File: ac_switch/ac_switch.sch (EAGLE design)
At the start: 7 parts, among them IC1 LM358D, T1 BC337

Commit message: schaltung AC-Switch 98% fertig
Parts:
- added C3, C5: 100n, resistor:C-EU025-024X044
- added C4: 470µ, resistor:CPOL-EUE2.5-7
- added LED1: (no value), led:LED5MM
- added LSP1, LSP2, LSP3, LSP4, LSP5, LSP6: SE14, solpad:SE14
- added R1: 10K, resistor:R-EU_0207/10
- added R2: 150R, resistor:R-EU_0207/10
- added U$3: I3C_PORT, n39:I3C_PORT
- added U$4: AVR_ISP, n39:AVR_ISP
- added X1: SSW-103-02-S-S-RA, con-samtec:SSW-103-02-S-S-RA
- IC1: value LM358D -> TINY85; device linear:LM358D -> atmel:TINY22P
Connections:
- new net L: LSP1.MP, LSP4.MP, U$2.IP+
- new net L_OUT: U$1.P$3, X1-3.1
- new net N: LSP2.MP, LSP5.MP, X1-2.1
- new net N$5: LED1.A, R2.2
- new net P: LSP3.MP, LSP6.MP, X1-1.1
- new net REQ: IC1.(MISO)PB1, U$3.REQ, U$4.MISO
- new net RST: IC1.RESET, R1.2, U$4.RST
- new net SCL: IC1.(SCK)PB2, U$3.SCL, U$4.SCK
- new net SDA: IC1.(MOSI)PB0, U$3.SDA, U$4.MOSI
- net GND: now also C3.1, C4.-, C5.2, IC1.GND, LED1.C
- net N$1: now also R2.1
- net SENSE: now also IC1.(CLOCK)PB3
- net SWITCH: now also IC1.PB4
- net VCC: now also C3.2, C4.+, C5.1, IC1.VCC, R1.1
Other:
- note added: "230VAC"
- note added: "5VDC"
- note removed: "Schmitt-Trigger 0.3V"

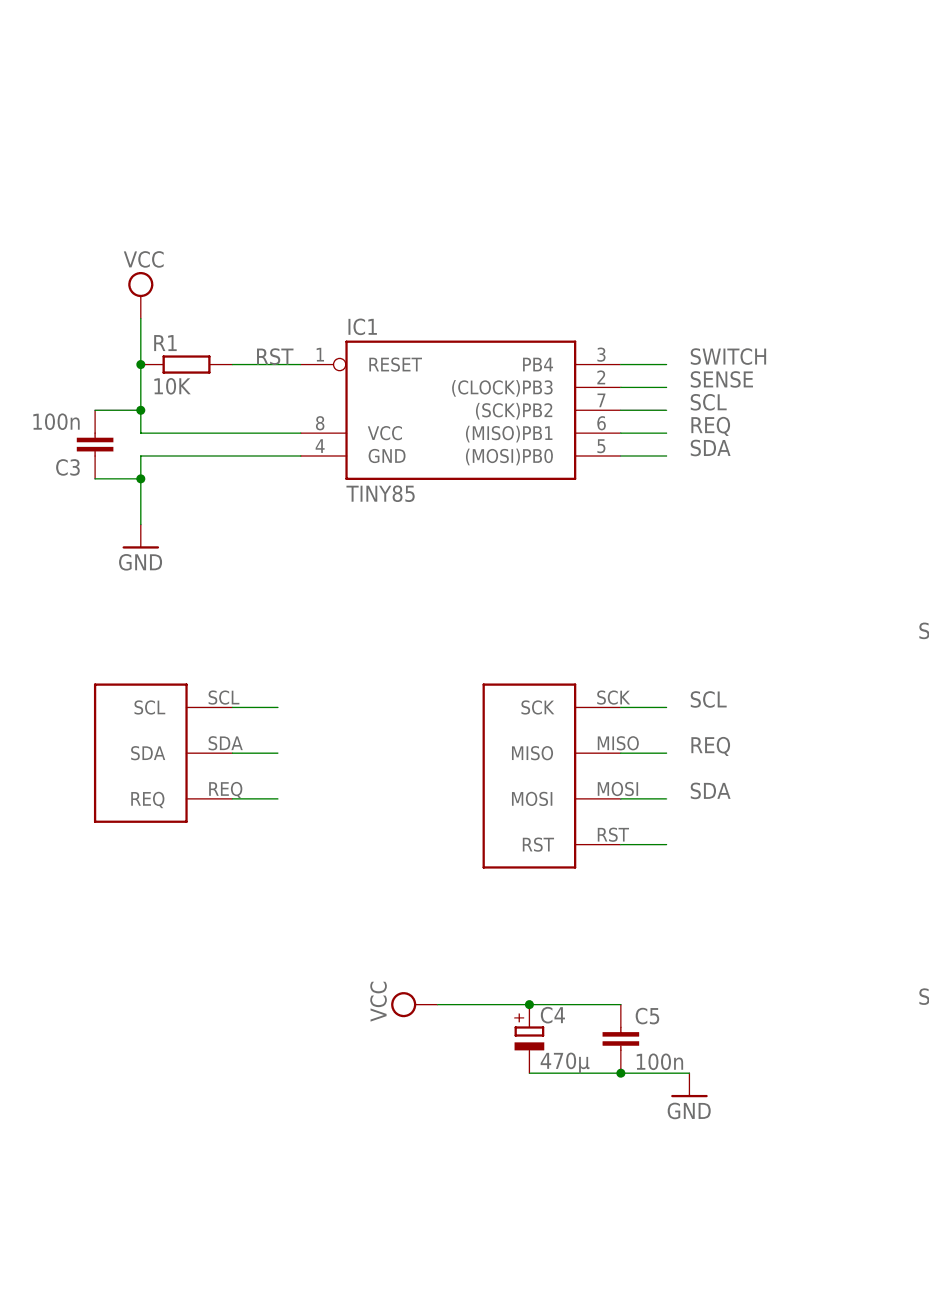
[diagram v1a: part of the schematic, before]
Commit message: weiterer I³C-Port
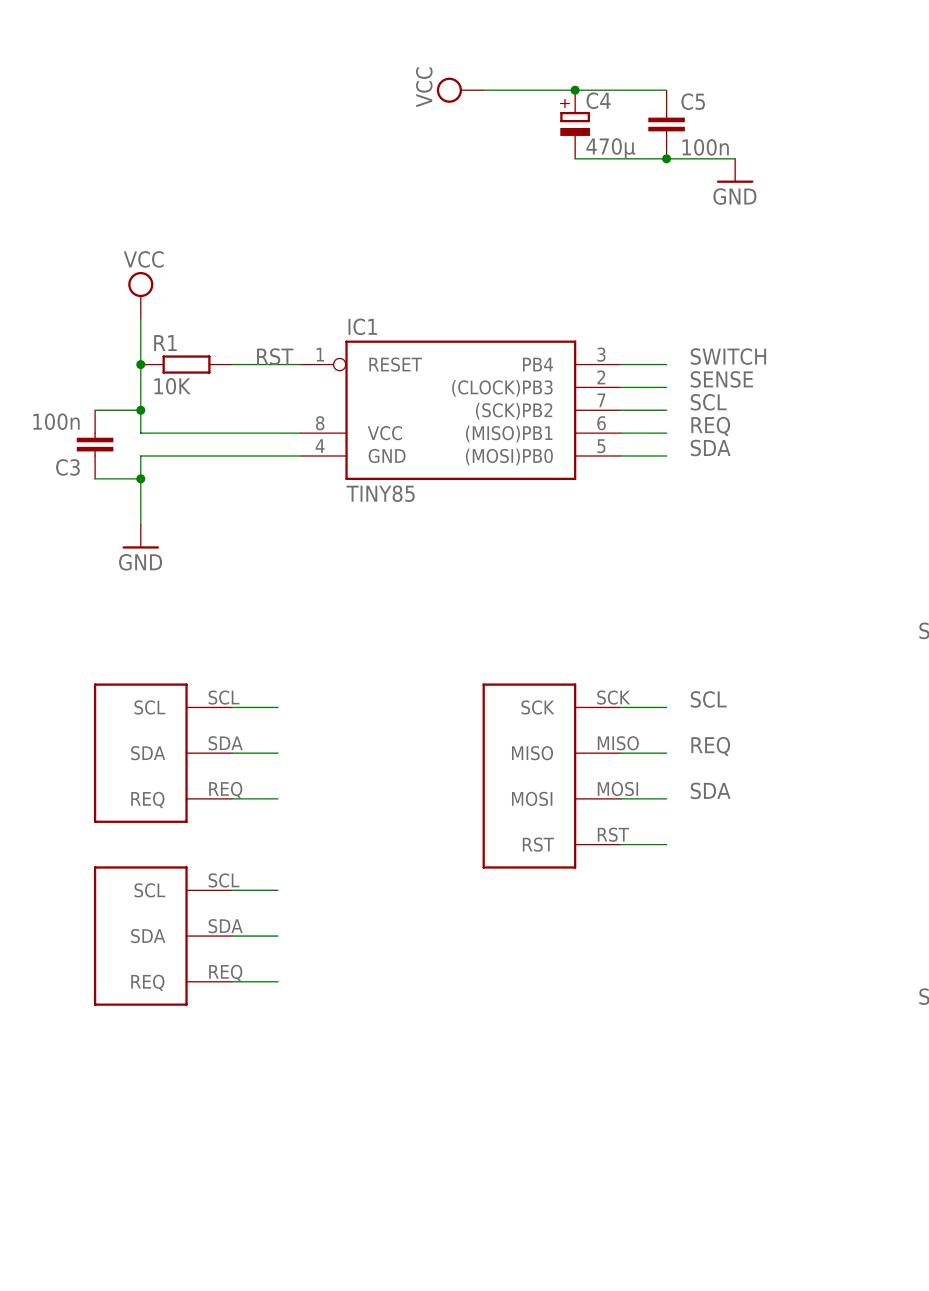
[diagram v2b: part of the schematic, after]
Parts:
- added U$5: I3C_PORT, n39:I3C_PORT
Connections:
- net REQ: now also U$5.REQ
- net SCL: now also U$5.SCL
- net SDA: now also U$5.SDA
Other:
- moved on the sheet: C4, C5
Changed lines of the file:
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@@
 <part name="C4" library="resistor" deviceset="CPOL-EU" device="E2.5-7" value="470µ"/>
 <part name="C5" library="resistor" deviceset="C-EU" device="025-024X044" value="100n"/>
+<part name="U$5" library="n39" deviceset="I3C_PORT" device=""/>
 </parts>
 <sheets>
@@
 <instance part="LSP6" gate="1" x="119.38" y="35.56" rot="R180"/>
 <instance part="GND1" gate="1" x="50.8" y="-38.1"/>
-<instance part="GND4" gate="1" x="0" y="-33.02"/>
-<instance part="SUPPLY4" gate="G$1" x="-30.48" y="-22.86" rot="R90"/>
-<instance part="C4" gate="G$1" x="-17.78" y="-25.4"/>
-<instance part="C5" gate="G$1" x="-7.62" y="-25.4"/>
+<instance part="GND4" gate="1" x="5.08" y="68.58"/>
+<instance part="SUPPLY4" gate="G$1" x="-25.4" y="78.74" rot="R90"/>
+<instance part="C4" gate="G$1" x="-12.7" y="76.2"/>
+<instance part="C5" gate="G$1" x="-2.54" y="76.2"/>
+<instance part="U$5" gate="G$1" x="-60.96" y="-17.78"/>
 </instances>
 <busses>
@@
 <pinref part="SUPPLY4" gate="G$1" pin="VCC"/>
 <pinref part="C4" gate="G$1" pin="+"/>
-<wire x1="-27.94" y1="-22.86" x2="-17.78" y2="-22.86" width="0.1524" layer="91"/>
-<wire x1="-17.78" y1="-22.86" x2="-7.62" y2="-22.86" width="0.1524" layer="91"/>
-<junction x="-17.78" y="-22.86"/>
+<wire x1="-22.86" y1="78.74" x2="-12.7" y2="78.74" width="0.1524" layer="91"/>
+<wire x1="-12.7" y1="78.74" x2="-2.54" y2="78.74" width="0.1524" layer="91"/>
+<junction x="-12.7" y="78.74"/>
 <pinref part="C5" gate="G$1" pin="1"/>
 </segment>
@@
 <pinref part="C4" gate="G$1" pin="-"/>
 <pinref part="GND4" gate="1" pin="GND"/>
-<wire x1="-17.78" y1="-30.48" x2="-7.62" y2="-30.48" width="0.1524" layer="91"/>
+<wire x1="-12.7" y1="71.12" x2="-2.54" y2="71.12" width="0.1524" layer="91"/>
 <pinref part="C5" gate="G$1" pin="2"/>
-<wire x1="-7.62" y1="-30.48" x2="0" y2="-30.48" width="0.1524" layer="91"/>
-<junction x="-7.62" y="-30.48"/>
+<wire x1="-2.54" y1="71.12" x2="5.08" y2="71.12" width="0.1524" layer="91"/>
+<junction x="-2.54" y="71.12"/>
 </segment>
 </net>
@@
 <label x="0" y="10.16" size="1.778" layer="95"/>
 </segment>
+<segment>
+<pinref part="U$5" gate="G$1" pin="SCL"/>
+<wire x1="-50.8" y1="-10.16" x2="-45.72" y2="-10.16" width="0.1524" layer="91"/>
+</segment>
 </net>
 <net name="REQ" class="0">
@@
 <label x="0" y="5.08" size="1.778" layer="95"/>
 </segment>
+<segment>
+<pinref part="U$5" gate="G$1" pin="REQ"/>
+<wire x1="-50.8" y1="-20.32" x2="-45.72" y2="-20.32" width="0.1524" layer="91"/>
+</segment>
 </net>
 <net name="SDA" class="0">
@@
 <label x="0" y="0" size="1.778" layer="95"/>
 </segment>
-</net>
+<segment>
+<pinref part="U$5" gate="G$1" pin="SDA"/>
+<wire x1="-50.8" y1="-15.24" x2="-45.72" y2="-15.24" width="0.1524" layer="91"/>
+</segment>
+</net>

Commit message: PCB-Routing
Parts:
- removed C5: 100n, resistor:C-EU025-024X044
- removed LSP3, LSP6: SE14, solpad:SE14
- removed X1: SSW-103-02-S-S-RA, con-samtec:SSW-103-02-S-S-RA
- added X2: SSW-102-02-S-S-RA, con-samtec:SSW-102-02-S-S-RA
- R2: device resistor:R-EU_0207/10 -> resistor:R-EU_0204/7
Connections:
- removed net P: LSP3.MP, LSP6.MP, X1-1.1
- net GND: no longer C5.2
- net L: now also U$2.IP-; no longer U$2.IP+
- net L_OUT: now also X2-1.1; no longer X1-3.1
- net N: now also X2-2.1; no longer X1-2.1
- net N$3: now also U$2.IP+; no longer U$2.IP-
- net VCC: no longer C5.1
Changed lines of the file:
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@@
 <part name="R1" library="resistor" deviceset="R-EU_" device="0207/10" value="10K"/>
 <part name="LED1" library="led" deviceset="LED" device="5MM"/>
-<part name="R2" library="resistor" deviceset="R-EU_" device="0207/10" value="150R"/>
+<part name="R2" library="resistor" deviceset="R-EU_" device="0204/7" value="150R"/>
 <part name="U$3" library="n39" deviceset="I3C_PORT" device=""/>
 <part name="U$4" library="n39" deviceset="AVR_ISP" device=""/>
-<part name="X1" library="con-samtec" deviceset="SSW-103-02-S-S" device="-RA"/>
 <part name="LSP1" library="solpad" deviceset="SE14" device=""/>
 <part name="LSP2" library="solpad" deviceset="SE14" device=""/>
-<part name="LSP3" library="solpad" deviceset="SE14" device=""/>
 <part name="LSP4" library="solpad" deviceset="SE14" device=""/>
 <part name="LSP5" library="solpad" deviceset="SE14" device=""/>
-<part name="LSP6" library="solpad" deviceset="SE14" device=""/>
 <part name="GND1" library="supply1" deviceset="GND" device=""/>
 <part name="GND4" library="supply1" deviceset="GND" device=""/>
 <part name="SUPPLY4" library="supply2" deviceset="VCC" device=""/>
 <part name="C4" library="resistor" deviceset="CPOL-EU" device="E2.5-7" value="470µ"/>
-<part name="C5" library="resistor" deviceset="C-EU" device="025-024X044" value="100n"/>
 <part name="U$5" library="n39" deviceset="I3C_PORT" device=""/>
+<part name="X2" library="con-samtec" deviceset="SSW-102-02-S-S" device="-RA"/>
 </parts>
 <sheets>
@@
 <instance part="U$3" gate="G$1" x="-60.96" y="2.54"/>
 <instance part="U$4" gate="G$1" x="-10.16" y="2.54"/>
-<instance part="X1" gate="-1" x="129.54" y="5.08" rot="R180"/>
-<instance part="X1" gate="-2" x="129.54" y="7.62" rot="R180"/>
-<instance part="X1" gate="-3" x="129.54" y="10.16" rot="R180"/>
 <instance part="LSP1" gate="1" x="129.54" y="63.5"/>
 <instance part="LSP2" gate="1" x="124.46" y="63.5"/>
-<instance part="LSP3" gate="1" x="119.38" y="63.5"/>
 <instance part="LSP4" gate="1" x="129.54" y="35.56" rot="R180"/>
 <instance part="LSP5" gate="1" x="124.46" y="35.56" rot="R180"/>
-<instance part="LSP6" gate="1" x="119.38" y="35.56" rot="R180"/>
 <instance part="GND1" gate="1" x="50.8" y="-38.1"/>
 <instance part="GND4" gate="1" x="5.08" y="68.58"/>
 <instance part="SUPPLY4" gate="G$1" x="-25.4" y="78.74" rot="R90"/>
 <instance part="C4" gate="G$1" x="-12.7" y="76.2"/>
-<instance part="C5" gate="G$1" x="-2.54" y="76.2"/>
 <instance part="U$5" gate="G$1" x="-60.96" y="-17.78"/>
+<instance part="X2" gate="-1" x="129.54" y="20.32" rot="R180"/>
+<instance part="X2" gate="-2" x="129.54" y="22.86" rot="R180"/>
 </instances>
 <busses>
@@
 </segment>
 </net>
-<net name="N$3" class="0">
-<segment>
-<pinref part="U$2" gate="ACS714" pin="IP-"/>
-<pinref part="U$1" gate="G$1" pin="P$4"/>
-<wire x1="78.74" y1="-5.08" x2="78.74" y2="30.48" width="0.1524" layer="91"/>
-</segment>
-</net>
 <net name="VCC" class="0">
 <segment>
@@
 <pinref part="C4" gate="G$1" pin="+"/>
 <wire x1="-22.86" y1="78.74" x2="-12.7" y2="78.74" width="0.1524" layer="91"/>
-<wire x1="-12.7" y1="78.74" x2="-2.54" y2="78.74" width="0.1524" layer="91"/>
-<junction x="-12.7" y="78.74"/>
-<pinref part="C5" gate="G$1" pin="1"/>
 </segment>
 </net>
@@
 <pinref part="C4" gate="G$1" pin="-"/>
 <pinref part="GND4" gate="1" pin="GND"/>
-<wire x1="-12.7" y1="71.12" x2="-2.54" y2="71.12" width="0.1524" layer="91"/>
-<pinref part="C5" gate="G$1" pin="2"/>
-<wire x1="-2.54" y1="71.12" x2="5.08" y2="71.12" width="0.1524" layer="91"/>
-<junction x="-2.54" y="71.12"/>
+<wire x1="-12.7" y1="71.12" x2="5.08" y2="71.12" width="0.1524" layer="91"/>
 </segment>
 </net>
@@
 </segment>
 </net>
-<net name="L_OUT" class="0">
-<segment>
-<pinref part="U$1" gate="G$1" pin="P$3"/>
-<wire x1="73.66" y1="53.34" x2="91.44" y2="53.34" width="0.1524" layer="91"/>
-<label x="96.52" y="53.34" size="1.778" layer="95"/>
-</segment>
-<segment>
-<pinref part="X1" gate="-3" pin="1"/>
-<wire x1="127" y1="10.16" x2="121.92" y2="10.16" width="0.1524" layer="91"/>
-<label x="119.38" y="10.16" size="1.778" layer="95"/>
-</segment>
-</net>
-<net name="P" class="0">
-<segment>
-<pinref part="LSP3" gate="1" pin="MP"/>
-<pinref part="LSP6" gate="1" pin="MP"/>
-<wire x1="119.38" y1="60.96" x2="119.38" y2="38.1" width="0.1524" layer="91"/>
-<label x="119.38" y="58.42" size="1.778" layer="95"/>
-</segment>
-<segment>
-<pinref part="X1" gate="-1" pin="1"/>
-<wire x1="127" y1="5.08" x2="121.92" y2="5.08" width="0.1524" layer="91"/>
-<label x="119.38" y="5.08" size="1.778" layer="95"/>
-</segment>
-</net>
 <net name="N" class="0">
 <segment>
@@
 </segment>
 <segment>
-<pinref part="X1" gate="-2" pin="1"/>
-<wire x1="127" y1="7.62" x2="121.92" y2="7.62" width="0.1524" layer="91"/>
-<label x="119.38" y="7.62" size="1.778" layer="95"/>
+<pinref part="X2" gate="-2" pin="1"/>
+<wire x1="127" y1="22.86" x2="124.46" y2="22.86" width="0.1524" layer="91"/>
+<label x="121.92" y="22.86" size="1.778" layer="95"/>
+</segment>
+</net>
+<net name="N$3" class="0">
+<segment>
+<pinref part="U$1" gate="G$1" pin="P$4"/>
+<wire x1="78.74" y1="30.48" x2="78.74" y2="5.08" width="0.1524" layer="91"/>
+<wire x1="78.74" y1="5.08" x2="88.9" y2="5.08" width="0.1524" layer="91"/>
+<wire x1="88.9" y1="5.08" x2="88.9" y2="-35.56" width="0.1524" layer="91"/>
+<pinref part="U$2" gate="ACS714" pin="IP+"/>
+<wire x1="88.9" y1="-35.56" x2="78.74" y2="-35.56" width="0.1524" layer="91"/>
 </segment>
 </net>
@@
 </segment>
 <segment>
-<pinref part="U$2" gate="ACS714" pin="IP+"/>
-<wire x1="78.74" y1="-35.56" x2="93.98" y2="-35.56" width="0.1524" layer="91"/>
-<label x="99.06" y="-35.56" size="1.778" layer="95"/>
-</segment>
-</net>
+<pinref part="U$2" gate="ACS714" pin="IP-"/>
+<wire x1="78.74" y1="-5.08" x2="93.98" y2="-5.08" width="0.1524" layer="91"/>
+<label x="96.52" y="-5.08" size="1.778" layer="95"/>
+</segment>
+</net>
+<net name="L_OUT" class="0">
+<segment>
+<pinref part="U$1" gate="G$1" pin="P$3"/>
+<wire x1="73.66" y1="53.34" x2="93.98" y2="53.34" width="0.1524" layer="91"/>
+<label x="96.52" y="53.34" size="1.778" layer="95"/>
+</segment>
+<segment>
+<pinref part="X2" gate="-1" pin="1"/>
+<wire x1="127" y1="20.32" x2="124.46" y2="20.32" width="0.1524" layer="91"/>
+<label x="116.84" y="20.32" size="1.778" layer="95"/>
+</segment>
+</net>
